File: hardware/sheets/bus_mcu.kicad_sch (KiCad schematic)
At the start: 20 parts, among them M1 Core2350B (0MB PSRAM), U10 74HCT163, U11 74HCT163, U12 74HCT165, U2 74LVC245A, U3 74LVC245A, U4 74LVC245A, U5 74LVC245A, U6 74LVC245A, U7 74HCT163, U8 74HCT163, U9 74HCT163

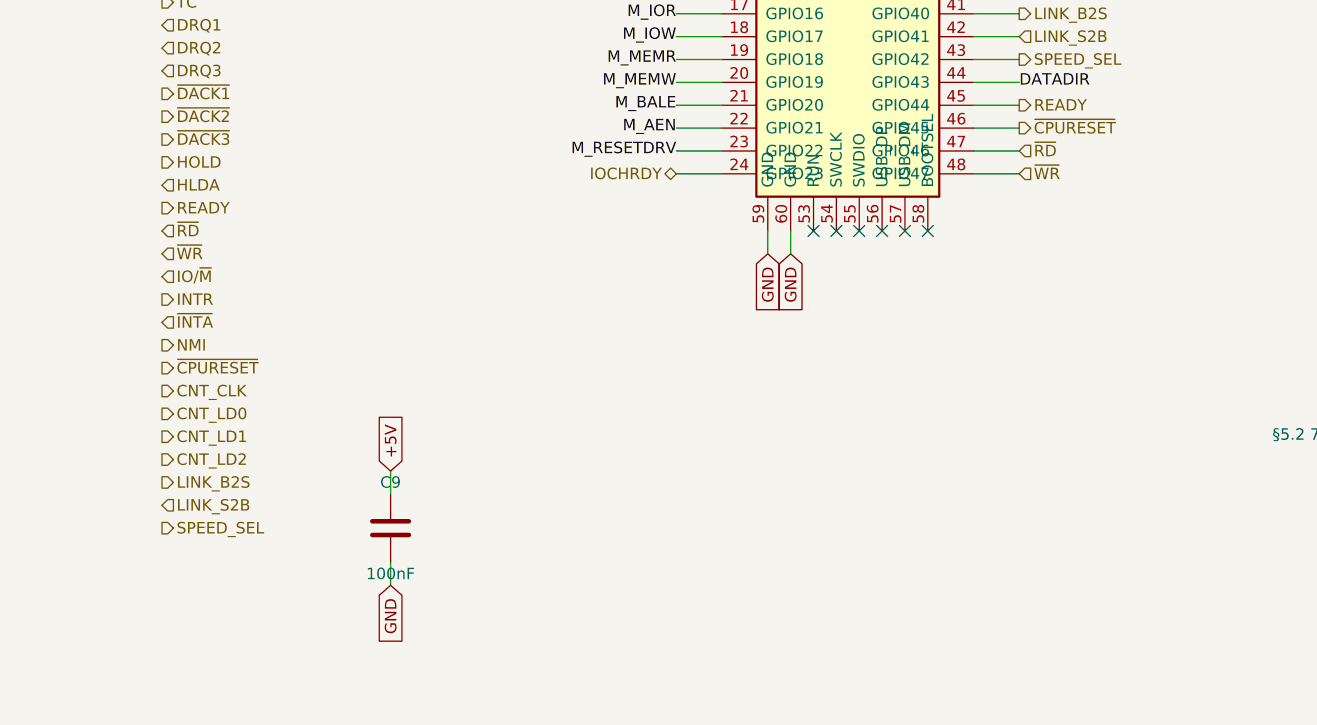
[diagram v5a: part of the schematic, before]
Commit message: Drive ISA REFRESH# from the Bus MCU for DRAM-based cards
Pin 35 (DACK0/REFRESH#) net renamed ~{DACK0} -> ~{REFRESH} in isa_conn and is now
an active Bus MCU output (GPIO47, reclaimed from the redundant raw-~WR sense -- the
MCU tracks writes via the gated MEMW/IOW). Driven from the internal ~15us refresh
timer (same source as the 0x61-bit-4 toggle); a refresh cycle reuses the bus-master
engine to walk the row address on A0-A7 + pulse MEMR#, so DRAM ISA cards see a
standard refresh. ~{REFRESH} added to the Bus MCU interface. Verified it ties
sidecar<->Bus MCU and passes through J_IN<->J_OUT on every dev card; zero
structural ERC on motherboard and all five cards.

Co-Authored-By: Claude Opus 4.8 (1M context) <noreply@anthropic.com>
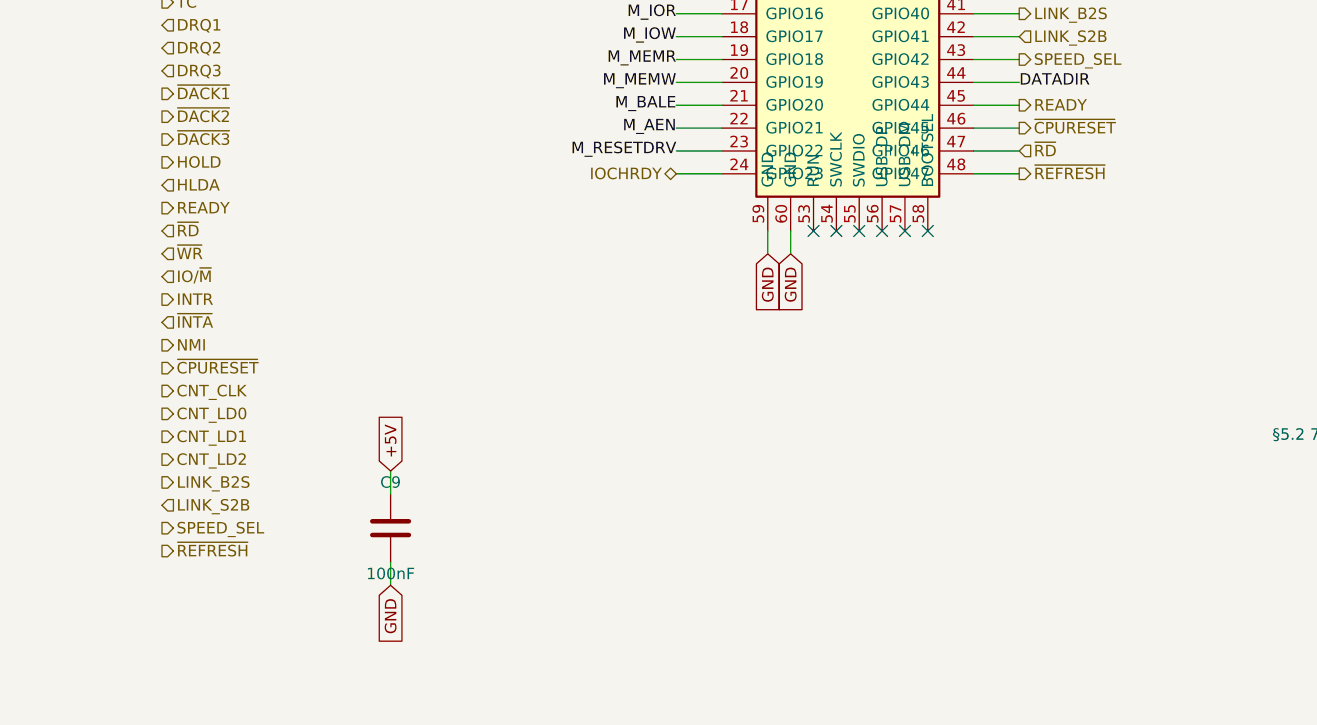
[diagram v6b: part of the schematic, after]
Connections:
- net ~{WR}: no longer M1.48 (GPIO47)
- new net ~{REFRESH}: M1.48 (GPIO47)
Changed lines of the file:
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@@
 		)
 	)
+	(hierarchical_label "~{REFRESH}"
+		(shape output)
+		(at 25.4 223.52 0)
+		(effects
+			(font
+				(size 1.27 1.27)
+			)
+		)
+	)
 	(wire
 		(pts
@@
 		)
 	)
-	(hierarchical_label "~{WR}"
-		(shape input)
+	(hierarchical_label "~{REFRESH}"
+		(shape output)
 		(at 120.65 181.61 0)
 		(effects
@@
 		(instances
 			(project "mini-xt"
-				(path "/9602cc72-403c-4cc6-86da-e35dd0751fe2/a91b0290-01c2-43ab-b8ab-8f8d8ddc9ec8"
+				(path "/442cfbd8-63ab-49e7-b08c-2cb3161d8599/9c25c518-4bf8-4983-82be-0df8a99a8e33"
 					(reference "M201")
 					(unit 1)
@@
 		(instances
 			(project "mini-xt"
-				(path "/9602cc72-403c-4cc6-86da-e35dd0751fe2/a91b0290-01c2-43ab-b8ab-8f8d8ddc9ec8"
+				(path "/442cfbd8-63ab-49e7-b08c-2cb3161d8599/9c25c518-4bf8-4983-82be-0df8a99a8e33"
 					(reference "U202")
 					(unit 1)
@@
 		(instances
 			(project "mini-xt"
-				(path "/9602cc72-403c-4cc6-86da-e35dd0751fe2/a91b0290-01c2-43ab-b8ab-8f8d8ddc9ec8"
+				(path "/442cfbd8-63ab-49e7-b08c-2cb3161d8599/9c25c518-4bf8-4983-82be-0df8a99a8e33"
 					(reference "U206")
 					(unit 1)
@@
 		(instances
 			(project "mini-xt"
-				(path "/9602cc72-403c-4cc6-86da-e35dd0751fe2/a91b0290-01c2-43ab-b8ab-8f8d8ddc9ec8"
+				(path "/442cfbd8-63ab-49e7-b08c-2cb3161d8599/9c25c518-4bf8-4983-82be-0df8a99a8e33"
 					(reference "U203")
 					(unit 1)
@@
 		(instances
 			(project "mini-xt"
-				(path "/9602cc72-403c-4cc6-86da-e35dd0751fe2/a91b0290-01c2-43ab-b8ab-8f8d8ddc9ec8"
+				(path "/442cfbd8-63ab-49e7-b08c-2cb3161d8599/9c25c518-4bf8-4983-82be-0df8a99a8e33"
 					(reference "U204")
 					(unit 1)
@@
 		(instances
 			(project "mini-xt"
-				(path "/9602cc72-403c-4cc6-86da-e35dd0751fe2/a91b0290-01c2-43ab-b8ab-8f8d8ddc9ec8"
+				(path "/442cfbd8-63ab-49e7-b08c-2cb3161d8599/9c25c518-4bf8-4983-82be-0df8a99a8e33"
 					(reference "U205")
 					(unit 1)
@@
 		(instances
 			(project "mini-xt"
-				(path "/9602cc72-403c-4cc6-86da-e35dd0751fe2/a91b0290-01c2-43ab-b8ab-8f8d8ddc9ec8"
+				(path "/442cfbd8-63ab-49e7-b08c-2cb3161d8599/9c25c518-4bf8-4983-82be-0df8a99a8e33"
 					(reference "U207")
 					(unit 1)
@@
 		(instances
 			(project "mini-xt"
-				(path "/9602cc72-403c-4cc6-86da-e35dd0751fe2/a91b0290-01c2-43ab-b8ab-8f8d8ddc9ec8"
+				(path "/442cfbd8-63ab-49e7-b08c-2cb3161d8599/9c25c518-4bf8-4983-82be-0df8a99a8e33"
 					(reference "U208")
 					(unit 1)
@@
 		(instances
 			(project "mini-xt"
-				(path "/9602cc72-403c-4cc6-86da-e35dd0751fe2/a91b0290-01c2-43ab-b8ab-8f8d8ddc9ec8"
+				(path "/442cfbd8-63ab-49e7-b08c-2cb3161d8599/9c25c518-4bf8-4983-82be-0df8a99a8e33"
 					(reference "U209")
 					(unit 1)
@@
 		(instances
 			(project "mini-xt"
-				(path "/9602cc72-403c-4cc6-86da-e35dd0751fe2/a91b0290-01c2-43ab-b8ab-8f8d8ddc9ec8"
+				(path "/442cfbd8-63ab-49e7-b08c-2cb3161d8599/9c25c518-4bf8-4983-82be-0df8a99a8e33"
 					(reference "U210")
 					(unit 1)
@@
 		(instances
 			(project "mini-xt"
-				(path "/9602cc72-403c-4cc6-86da-e35dd0751fe2/a91b0290-01c2-43ab-b8ab-8f8d8ddc9ec8"
+				(path "/442cfbd8-63ab-49e7-b08c-2cb3161d8599/9c25c518-4bf8-4983-82be-0df8a99a8e33"
 					(reference "U211")
 					(unit 1)
@@
 		(instances
 			(project "mini-xt"
-				(path "/9602cc72-403c-4cc6-86da-e35dd0751fe2/a91b0290-01c2-43ab-b8ab-8f8d8ddc9ec8"
+				(path "/442cfbd8-63ab-49e7-b08c-2cb3161d8599/9c25c518-4bf8-4983-82be-0df8a99a8e33"
 					(reference "U212")
 					(unit 1)
@@
 		(instances
 			(project "mini-xt"
-				(path "/9602cc72-403c-4cc6-86da-e35dd0751fe2/a91b0290-01c2-43ab-b8ab-8f8d8ddc9ec8"
+				(path "/442cfbd8-63ab-49e7-b08c-2cb3161d8599/9c25c518-4bf8-4983-82be-0df8a99a8e33"
 					(reference "C201")
 					(unit 1)
@@
 		(instances
 			(project "mini-xt"
-				(path "/9602cc72-403c-4cc6-86da-e35dd0751fe2/a91b0290-01c2-43ab-b8ab-8f8d8ddc9ec8"
+				(path "/442cfbd8-63ab-49e7-b08c-2cb3161d8599/9c25c518-4bf8-4983-82be-0df8a99a8e33"
 					(reference "C202")
 					(unit 1)
@@
 		(instances
 			(project "mini-xt"
-				(path "/9602cc72-403c-4cc6-86da-e35dd0751fe2/a91b0290-01c2-43ab-b8ab-8f8d8ddc9ec8"
+				(path "/442cfbd8-63ab-49e7-b08c-2cb3161d8599/9c25c518-4bf8-4983-82be-0df8a99a8e33"
 					(reference "C203")
 					(unit 1)
@@
 		(instances
 			(project "mini-xt"
-				(path "/9602cc72-403c-4cc6-86da-e35dd0751fe2/a91b0290-01c2-43ab-b8ab-8f8d8ddc9ec8"
+				(path "/442cfbd8-63ab-49e7-b08c-2cb3161d8599/9c25c518-4bf8-4983-82be-0df8a99a8e33"
 					(reference "C206")
 					(unit 1)
@@
 		(instances
 			(project "mini-xt"
-				(path "/9602cc72-403c-4cc6-86da-e35dd0751fe2/a91b0290-01c2-43ab-b8ab-8f8d8ddc9ec8"
+				(path "/442cfbd8-63ab-49e7-b08c-2cb3161d8599/9c25c518-4bf8-4983-82be-0df8a99a8e33"
 					(reference "C207")
 					(unit 1)
@@
 		(instances
 			(project "mini-xt"
-				(path "/9602cc72-403c-4cc6-86da-e35dd0751fe2/a91b0290-01c2-43ab-b8ab-8f8d8ddc9ec8"
+				(path "/442cfbd8-63ab-49e7-b08c-2cb3161d8599/9c25c518-4bf8-4983-82be-0df8a99a8e33"
 					(reference "C208")
 					(unit 1)
@@
 		(instances
 			(project "mini-xt"
-				(path "/9602cc72-403c-4cc6-86da-e35dd0751fe2/a91b0290-01c2-43ab-b8ab-8f8d8ddc9ec8"
+				(path "/442cfbd8-63ab-49e7-b08c-2cb3161d8599/9c25c518-4bf8-4983-82be-0df8a99a8e33"
 					(reference "C209")
 					(unit 1)
@@
 		(instances
 			(project "mini-xt"
-				(path "/9602cc72-403c-4cc6-86da-e35dd0751fe2/a91b0290-01c2-43ab-b8ab-8f8d8ddc9ec8"
+				(path "/442cfbd8-63ab-49e7-b08c-2cb3161d8599/9c25c518-4bf8-4983-82be-0df8a99a8e33"
 					(reference "C210")
 					(unit 1)

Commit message: Fix all critical+high design-review findings (C1-C5, H1-H8)
Full review in hardware/notes/design-review-2026-07-03.md (with per-item
fix logs). Highlights:
- SRAM strobed by gated MEMR/MEMW (was raw ~RD/~WR: I/O cycles corrupted
  SRAM and the boot shadow-load could never write it)
- Reset chain implemented: NAND combine of ~PWRGOOD + ~CPURESET drives
  V20 RESET and an always-driven RESET_DRV (dropped from the Bus MCU)
- Contention-free bus handoff: '573 OE=HLDA vs counter '244 stage
  ~OE=~HLDA; strobe gates wired + tri-stated ('125, ~OE=HLDA); Bus MCU
  address group fixed to sense; AEN/TC fixed drive; BALE input-only
- '573 LE driven by BALE (was a dangling BALE_L label)
- Data '245 DIR=DT/~R, ~OE=DEN so INTA vectors reach the CPU
- Idle pulls: strobes/DEN high, AEN/IRQ2-9/DRQ low, IOCHRDY/IOCHCK/
  DACK2-3 high
- CH224K CFG1 left open (grounding it selects 9-20V, not 5V)
- XT-IDE INTRQ pull-down (pull-up parked IRQ5 asserted)
- LPT status bit7 = ~Busy via spare inverter (SPP semantics)
- Audio summer TL072 -> MCP6002 (RRIO; TL072 out of spec at +5V single
  supply)
- card_isatest: DUT P-FET gate to V5RAW + NPN driver (default off, can
  fully turn off); /3 divider TC->~PE reload actually wired

Overturned picks corrected in notes/questions-*.md. All sheets + cards
rebuilt; structural ERC = 0; fixes netlist-verified.

Co-Authored-By: Claude Fable 5 <noreply@anthropic.com>
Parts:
- added R1, R10, R11, R12, R13, R2, R3, R4, R5, R6, R7, R8, R9: 10k, symbol Device:R
- added U13: 74LVC245A, symbol mini-xt:74LVC245A
- added U14, U15, U16: 74HCT244, symbol mini-xt:74HCT244
- added U17: 74HCT04, symbol mini-xt:74HCT04
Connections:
- net +5V: now also R12.1, R13.1, R2.1, R3.1, U14.20 (VCC), U15.20 (VCC), U16.19 (2OE), U16.20 (VCC), U17.14 (VCC)
- net 3V3_BUS: now also U13.1 (A->B), U13.20 (VCC)
- net A0: now also U14.18 (1Y0); no longer U7.14 (Q0)
- net A1: now also U14.16 (1Y1); no longer U7.13 (Q1)
- net A10: now also U15.14 (1Y2); no longer U9.12 (Q2)
- net A11: now also U15.12 (1Y3); no longer U9.11 (Q3)
- net A12: now also U15.3 (2Y0); no longer U10.14 (Q0)
- net A13: now also U15.5 (2Y1); no longer U10.13 (Q1)
- net A14: now also U15.7 (2Y2); no longer U10.12 (Q2)
- net A15: now also U15.9 (2Y3); no longer U10.11 (Q3)
- net A16: now also U16.18 (1Y0); no longer U11.14 (Q0)
- net A17: now also U16.16 (1Y1); no longer U11.13 (Q1)
- net A18: now also U16.14 (1Y2); no longer U11.12 (Q2)
- net A19: now also U16.12 (1Y3); no longer U11.11 (Q3)
- net A2: now also U14.14 (1Y2); no longer U7.12 (Q2)
- net A3: now also U14.12 (1Y3); no longer U7.11 (Q3)
- net A4: now also U14.3 (2Y0); no longer U8.14 (Q0)
- net A5: now also U14.5 (2Y1); no longer U8.13 (Q1)
- net A6: now also U14.7 (2Y2); no longer U8.12 (Q2)
- net A7: now also U14.9 (2Y3); no longer U8.11 (Q3)
- net A8: now also U15.18 (1Y0); no longer U9.14 (Q0)
- net A9: now also U15.16 (1Y1); no longer U9.13 (Q1)
- net AEN: now also U13.18 (B0); no longer U6.14 (B4)
- net BALE: now also U5.14 (B4); no longer U6.11 (B7)
- net CLK: now also M1.23 (GPIO22)
- net GND: now also U3.1 (A->B), U4.1 (A->B), U5.1 (A->B), R1.2, R10.1, R11.1, R4.1, R5.1, R6.1, R7.1, R8.1, R9.1, U13.10 (GND), U13.19 (CE), U14.10 (GND), U15.10 (GND), U16.10 (GND), U16.11 (2A3), U16.13 (2A2), U16.15 (2A1), U16.17 (2A0), U17.7 (GND)
- net HLDA: now also U17.1 (P1); no longer U3.1 (A->B), U4.1 (A->B), U5.1 (A->B)
- net IOCHRDY: now also R2.2
- net IRQ2: now also R4.2
- net IRQ3: now also R5.2
- net IRQ4: now also R6.2
- net IRQ5: now also R7.2
- net IRQ6: now also R8.2
- net IRQ7: now also R9.2
- net IRQ8: now also R10.2
- net IRQ9: now also R11.2
- net M_AEN: now also R1.1, U13.2 (A0); no longer U6.6 (A4)
- net M_BALE: now also U5.6 (A4); no longer U6.9 (A7)
- net M_TC: now also U13.3 (A1); no longer U6.8 (A6)
- net TC: now also U13.17 (B1); no longer U6.12 (B6)
- net ~{DACK2}: now also R12.2
- net ~{DACK3}: now also R13.2
- net ~{IOCHCK}: now also R3.2
- net M_RESETDRV: no longer names the net of U6.7 (A5)
- net M_RESETDRV: no longer M1.23 (GPIO22)
- net RESET_DRV: no longer names the net of U6.13 (B5)
- new net CA0: U14.2 (1A0), U7.14 (Q0)
- new net CA1: U14.4 (1A1), U7.13 (Q1)
- new net CA10: U15.6 (1A2), U9.12 (Q2)
- new net CA11: U15.8 (1A3), U9.11 (Q3)
- new net CA12: U10.14 (Q0), U15.17 (2A0)
- new net CA13: U10.13 (Q1), U15.15 (2A1)
- new net CA14: U10.12 (Q2), U15.13 (2A2)
- new net CA15: U10.11 (Q3), U15.11 (2A3)
- new net CA16: U11.14 (Q0), U16.2 (1A0)
- new net CA17: U11.13 (Q1), U16.4 (1A1)
- new net CA18: U11.12 (Q2), U16.6 (1A2)
- new net CA19: U11.11 (Q3), U16.8 (1A3)
- new net CA2: U14.6 (1A2), U7.12 (Q2)
- new net CA3: U14.8 (1A3), U7.11 (Q3)
- new net CA4: U14.17 (2A0), U8.14 (Q0)
- new net CA5: U14.15 (2A1), U8.13 (Q1)
- new net CA6: U14.13 (2A2), U8.12 (Q2)
- new net CA7: U14.11 (2A3), U8.11 (Q3)
- new net CA8: U15.2 (1A0), U9.14 (Q0)
- new net CA9: U15.4 (1A1), U9.13 (Q1)
- new net ~{HLDA}: U14.1 (1OE), U14.19 (2OE), U15.1 (1OE), U15.19 (2OE), U16.1 (1OE), U17.2 (P2)
- no-connect marks 18 -> 50
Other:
- note added: "U3-U5 address+BALE = fixed sense; U13 AEN/TC = fixed drive (R1 idles AEN low)"
- note added: "U6 strobes DIR = HLDA (bus role, §5.2); DATADIR = data read/write dir;"
- note added: "counter->bus OE stage: '244 ~OE = ~HLDA (master only); '573s release via OE = HLDA"
- note removed: "Addr/ctrl DIR = HLDA (bus role, §5.2); DATADIR = data read/write dir"
